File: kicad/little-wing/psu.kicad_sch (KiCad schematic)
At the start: 9 parts, among them J1 ${ALTIUM_VALUE}, U1 ${ALTIUM_VALUE}

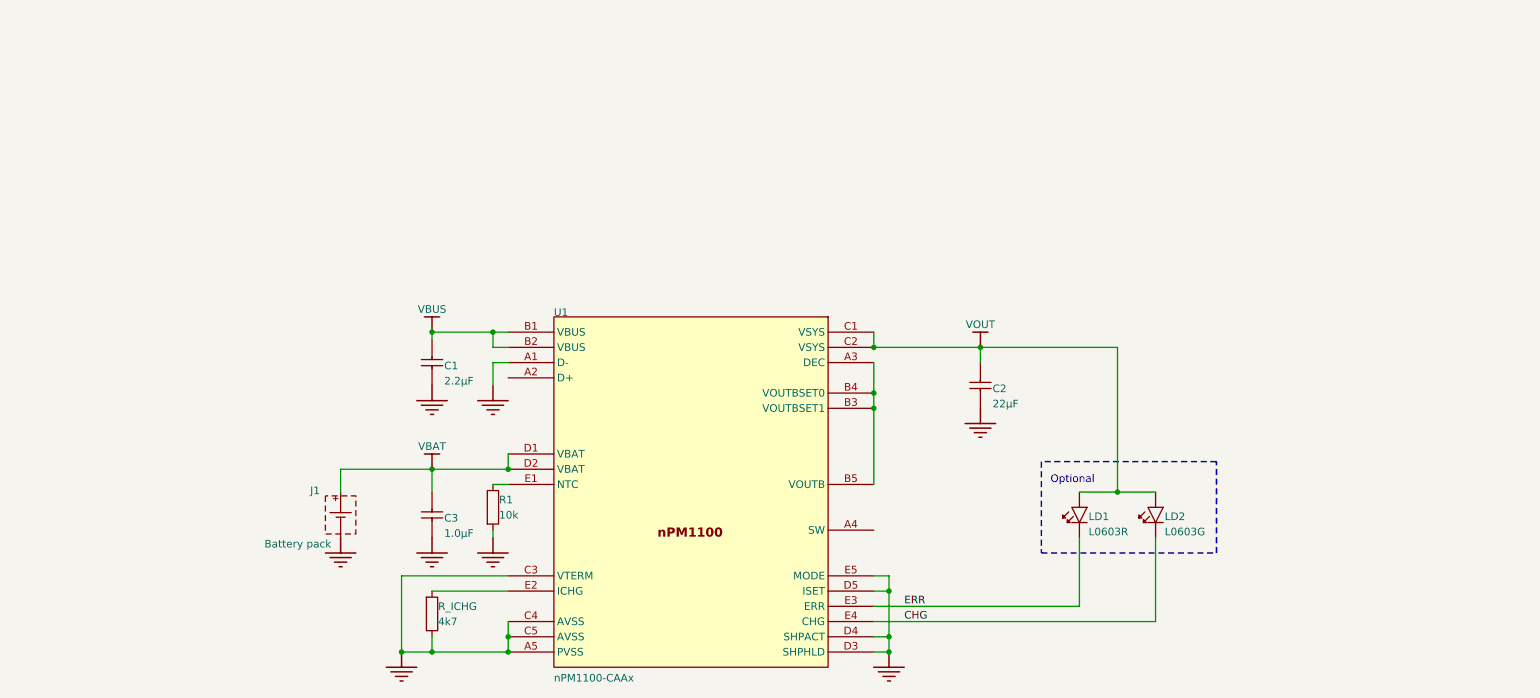
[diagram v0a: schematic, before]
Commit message: Re-shuffling the schematics across sub-sheets
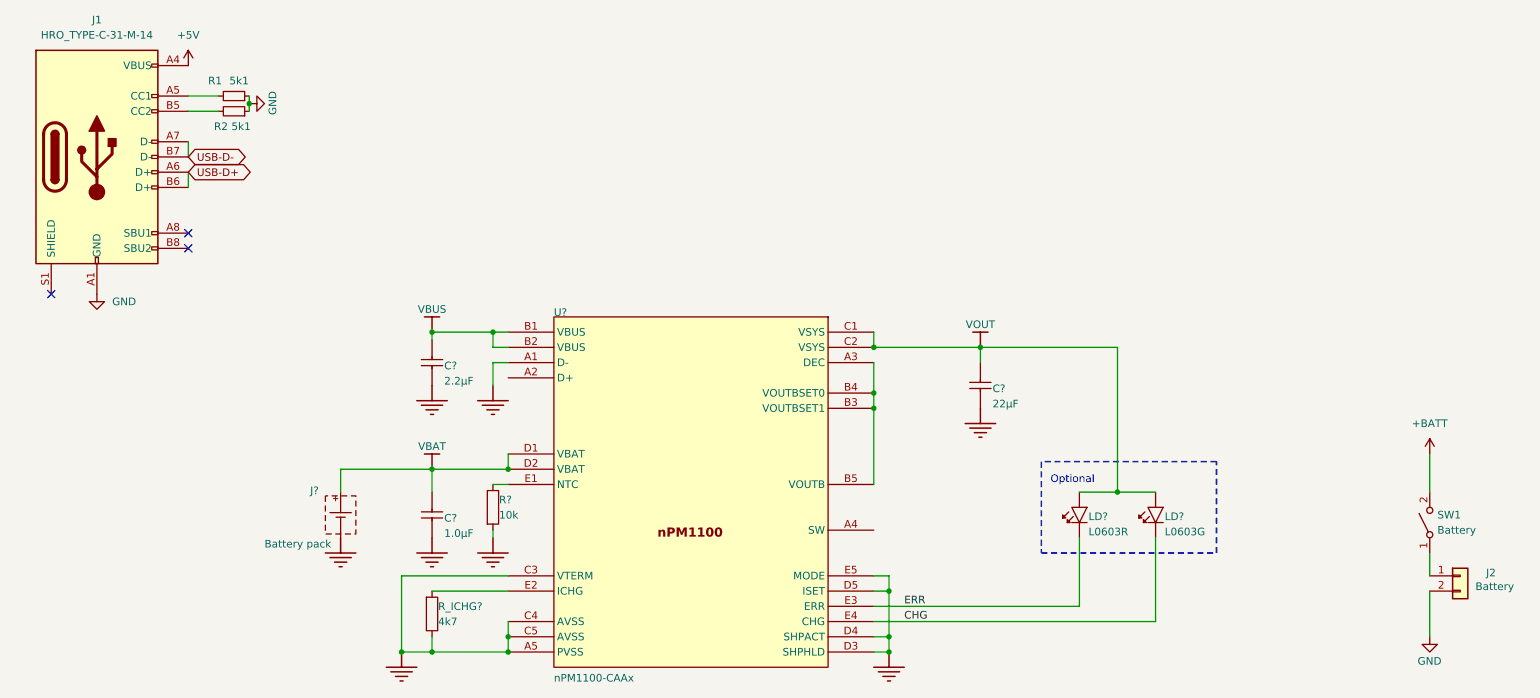
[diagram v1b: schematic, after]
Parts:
- added J1: HRO_TYPE-C-31-M-14, Connector_USB:USB_C_Receptacle_HRO_TYPE-C-31-M-12, symbol Connector:USB_C_Receptacle_USB2.0
- added J2: Battery, Connector_JST:JST_SH_SM02B-SRSS-TB_1x02-1MP_P1.00mm_Horizontal, symbol Connector_Generic:Conn_01x02
- added R1, R2: 5k1, Resistor_SMD:R_0402_1005Metric, symbol Device:R_Small
- added SW1: Battery, symbol Switch:SW_SPST
- renumbered C1 to C?, C2 to C?, C3 to C?, J1 to J?, LD1 to LD?, LD2 to LD?, R1 to R?, R_ICHG to R_ICHG?, U1 to U?
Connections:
- net GND: now also J1.A1 (GND), J1.A12 (GND), J1.B1 (GND), J1.B12 (GND), J2.2 (Pin_2), R1.1, R2.1
- new net: J2.1 (Pin_1), SW1.1 (A)
- new net: J1.A5 (CC1), R1.2
- new net: J1.B5 (CC2), R2.2
- new net +5V: J1.A4 (VBUS), J1.A9 (VBUS), J1.B4 (VBUS), J1.B9 (VBUS)
- new net +BATT: SW1.2 (B)
- new net USB-D+: J1.A6 (D+), J1.B6 (D+)
- new net USB-D-: J1.A7 (D-), J1.B7 (D-)
- no-connect marks 0 -> 3

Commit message: Tidying up the mess a little bit
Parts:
- removed J?: ${ALTIUM_VALUE}, TP_2x1mm_TH, symbol AltiumLib:root_0_Battery_pack_AltiumLib.DbLib
- gave numbers to parts that had none: 8
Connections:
- net +BATT is gone; now on net VBAT: SW1.2 (B)

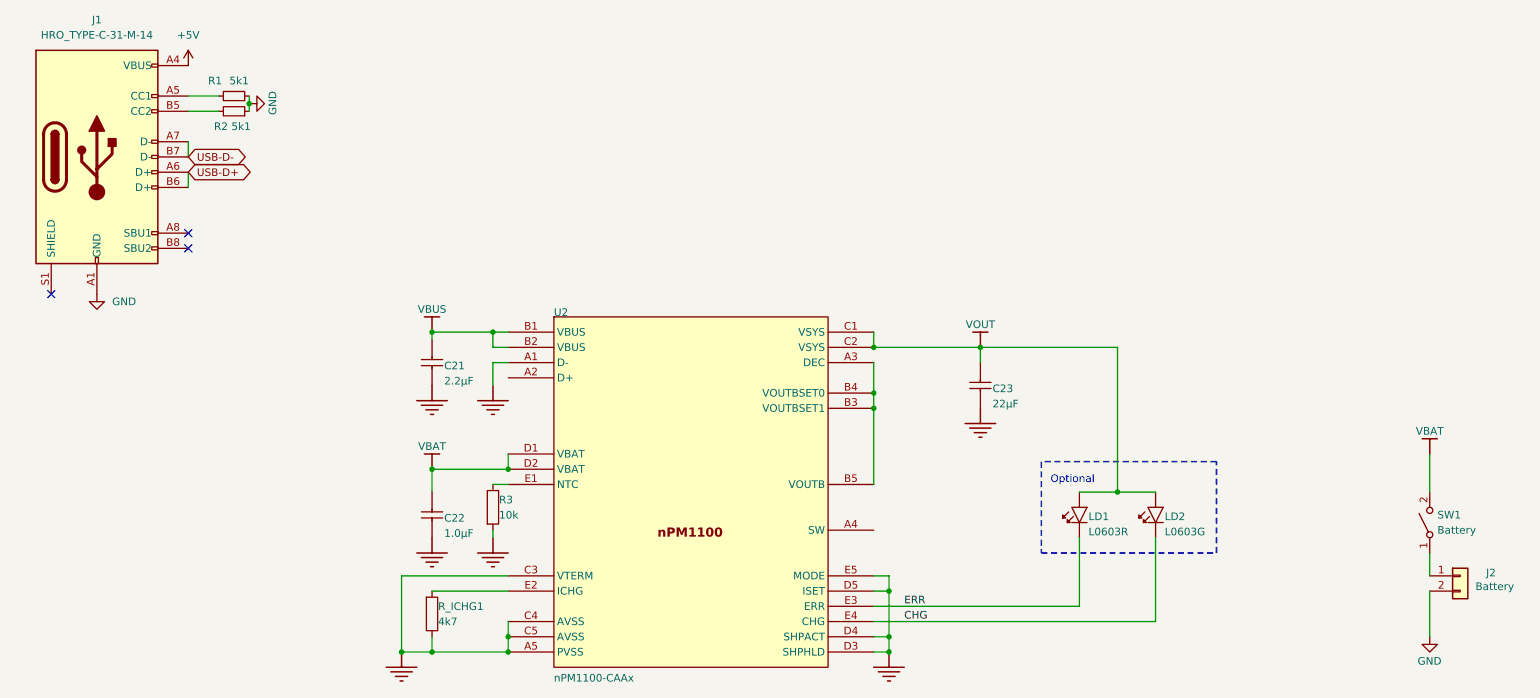
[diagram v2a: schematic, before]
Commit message: Cleaning up the PSU schematics
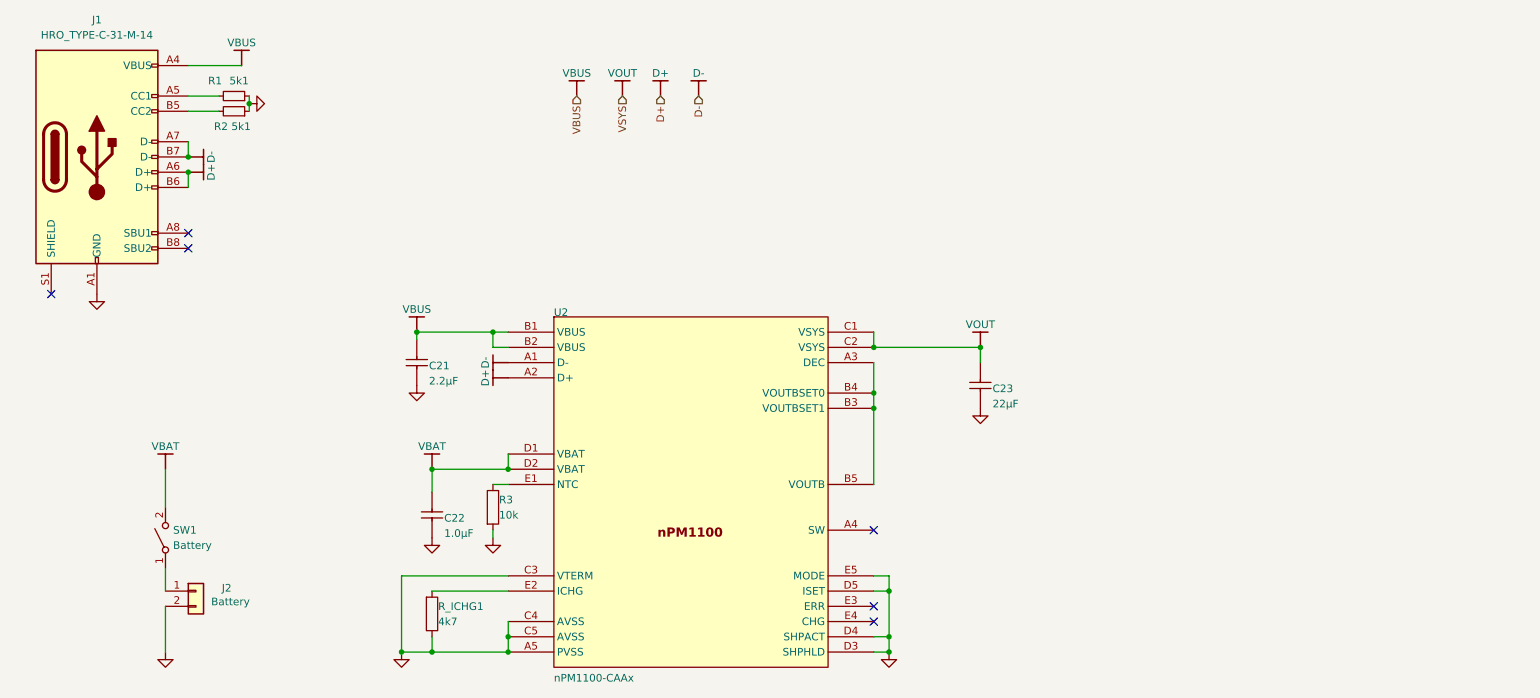
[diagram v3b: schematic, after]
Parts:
- removed LD1: ${ALTIUM_VALUE}, LED_0603_R, symbol AltiumLib:root_3_mirrored_D{colon}LED_AltiumLib.DbLib
- removed LD2: ${ALTIUM_VALUE}, LED_0603_G, symbol AltiumLib:root_3_mirrored_D{colon}LED_AltiumLib.DbLib
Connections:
- net +5V is gone; now on net VBUS: J1.A4 (VBUS), J1.A9 (VBUS), J1.B4 (VBUS), J1.B9 (VBUS)
- net USB-D+ is gone; now on net D+: J1.A6 (D+), J1.B6 (D+)
- net GND: no longer U2.A1 (D-)
- net D+: now reaches U2.A2 (D+)
- net CHG: no longer names the net of U2.E4 (CHG)
- net ERR: no longer names the net of U2.E3 (ERR)
- net USB-D- renamed D-
- net D-: now also U2.A1 (D-)
- no-connect marks 3 -> 6
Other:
- note removed: "Optional"
- moved on the sheet: C21, J2, SW1

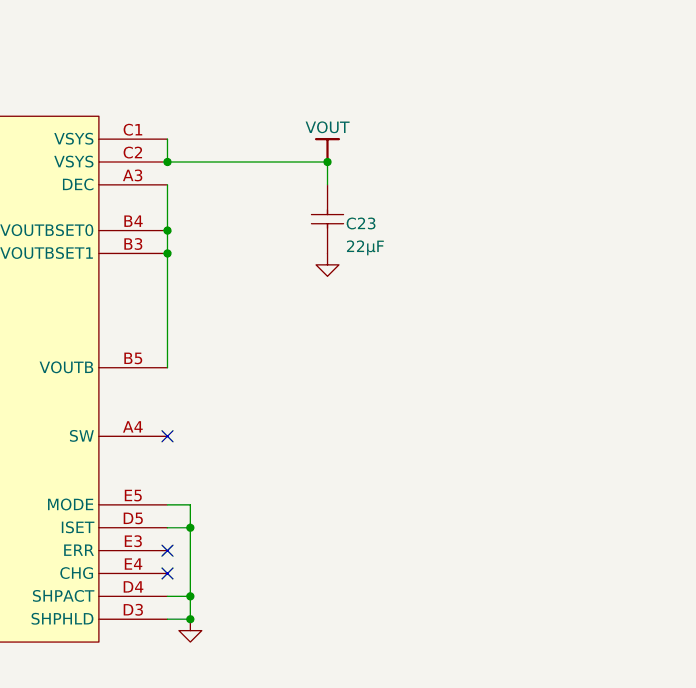
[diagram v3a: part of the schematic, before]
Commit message: Cleaning up the schematics a bit more
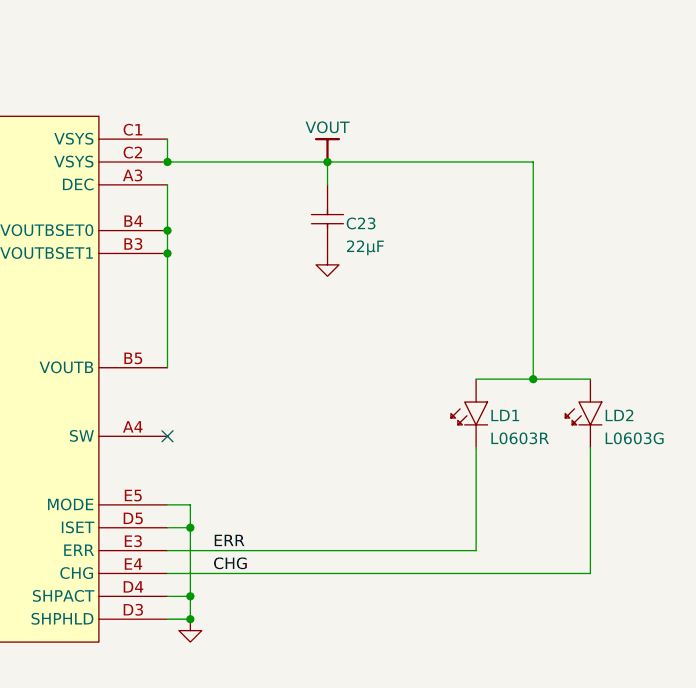
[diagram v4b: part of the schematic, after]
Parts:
- added LD1: ${ALTIUM_VALUE}, LED_0603_R, symbol AltiumLib:root_3_mirrored_D{colon}LED_AltiumLib.DbLib
- added LD2: ${ALTIUM_VALUE}, LED_0603_G, symbol AltiumLib:root_3_mirrored_D{colon}LED_AltiumLib.DbLib
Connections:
- net VOUT: now also LD1.2 (A), LD2.2 (A)
- net ERR: now reaches U2.E3 (ERR)
- net ERR: now also LD1.1 (C)
- net CHG: now reaches U2.E4 (CHG)
- net CHG: now also LD2.1 (C)
- no-connect marks 6 -> 4

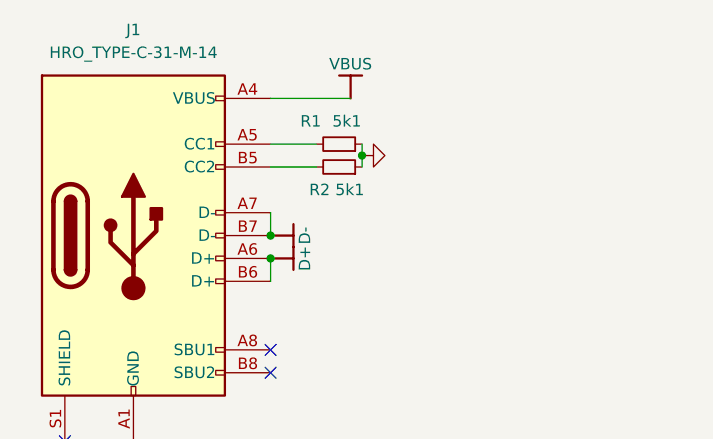
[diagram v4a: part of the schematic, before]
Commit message: Updating schematics/pcb to match the labels
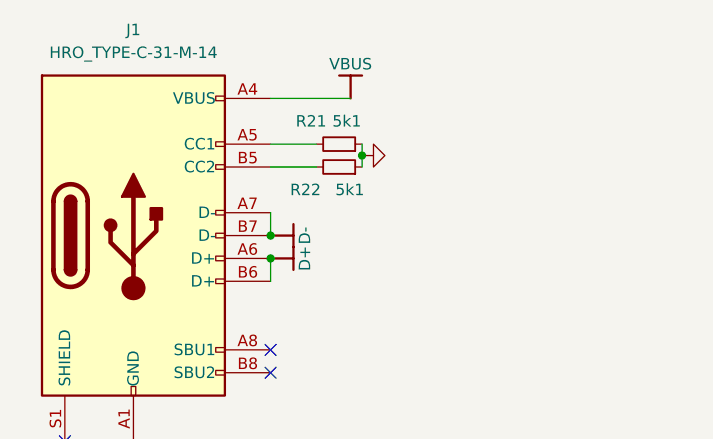
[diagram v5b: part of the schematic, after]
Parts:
- renumbered R1 to R21, R2 to R22
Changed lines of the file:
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@@
 		(on_board yes)
 		(dnp no)
-		(property "Reference" "R1"
-			(at 54.102 30.48 90)
+		(property "Reference" "R21"
+			(at 53.594 30.48 90)
 			(effects
 				(font
@@
 			(project "little-wing"
 				(path "/3a835e6f-a660-4b38-a102-87841cdd95ed/eaaf4618-ba3d-41b4-8a99-4f719e243661/4bfeadaf-0d2e-45fd-a340-a53ab79162c6"
-					(reference "R1")
+					(reference "R21")
 					(unit 1)
 				)
@@
 		(on_board yes)
 		(dnp no)
-		(property "Reference" "R2"
-			(at 57.404 38.1 90)
+		(property "Reference" "R22"
+			(at 56.388 38.1 90)
 			(effects
 				(font
@@
 			(project "little-wing"
 				(path "/3a835e6f-a660-4b38-a102-87841cdd95ed/eaaf4618-ba3d-41b4-8a99-4f719e243661/4bfeadaf-0d2e-45fd-a340-a53ab79162c6"
-					(reference "R2")
-					(unit 1)
-				)
+					(reference "R22")
+					(unit 1)
+				)

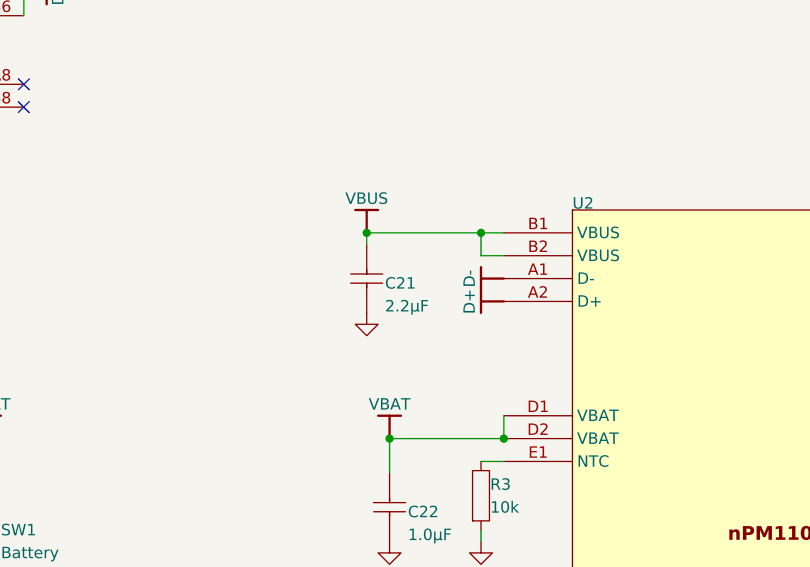
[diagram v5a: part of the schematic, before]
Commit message: Cleaning up some space on the PCB
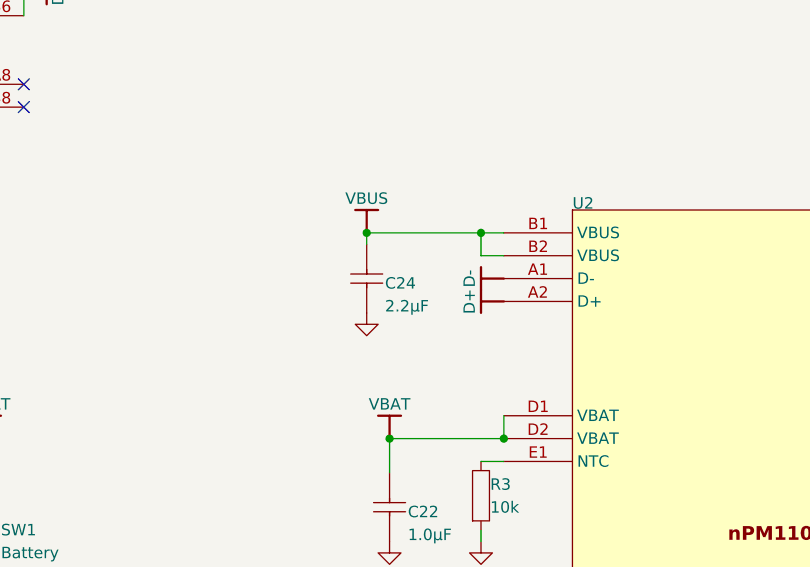
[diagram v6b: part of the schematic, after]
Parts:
- renumbered C21 to C24
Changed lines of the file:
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@@
 		(on_board yes)
 		(dnp no)
-		(property "Reference" "C21"
+		(property "Reference" "C24"
 			(at 90.932 78.74 0)
 			(effects
@@
 			(project "little-wing"
 				(path "/3a835e6f-a660-4b38-a102-87841cdd95ed/eaaf4618-ba3d-41b4-8a99-4f719e243661/4bfeadaf-0d2e-45fd-a340-a53ab79162c6"
-					(reference "C21")
+					(reference "C24")
 					(unit 1)
 				)

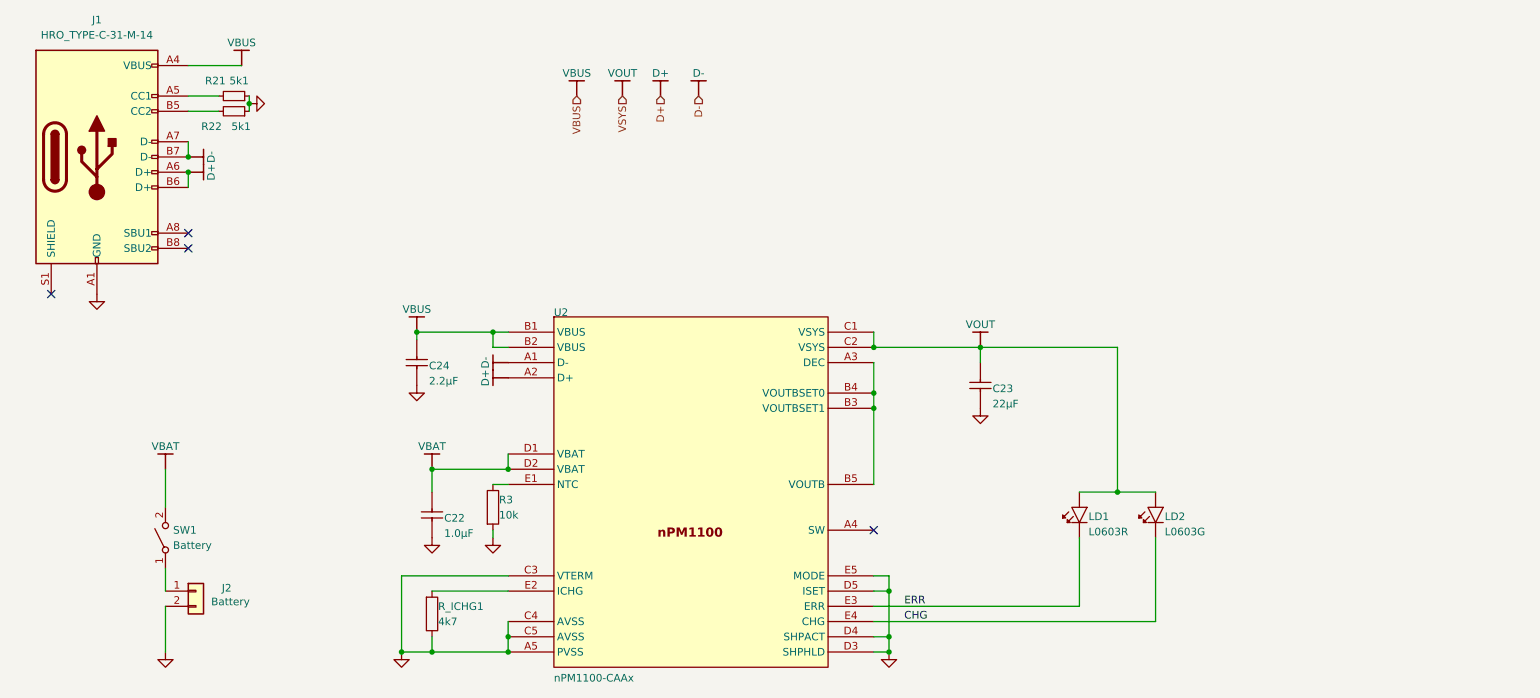
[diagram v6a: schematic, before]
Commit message: Reseting all the extra components sizes
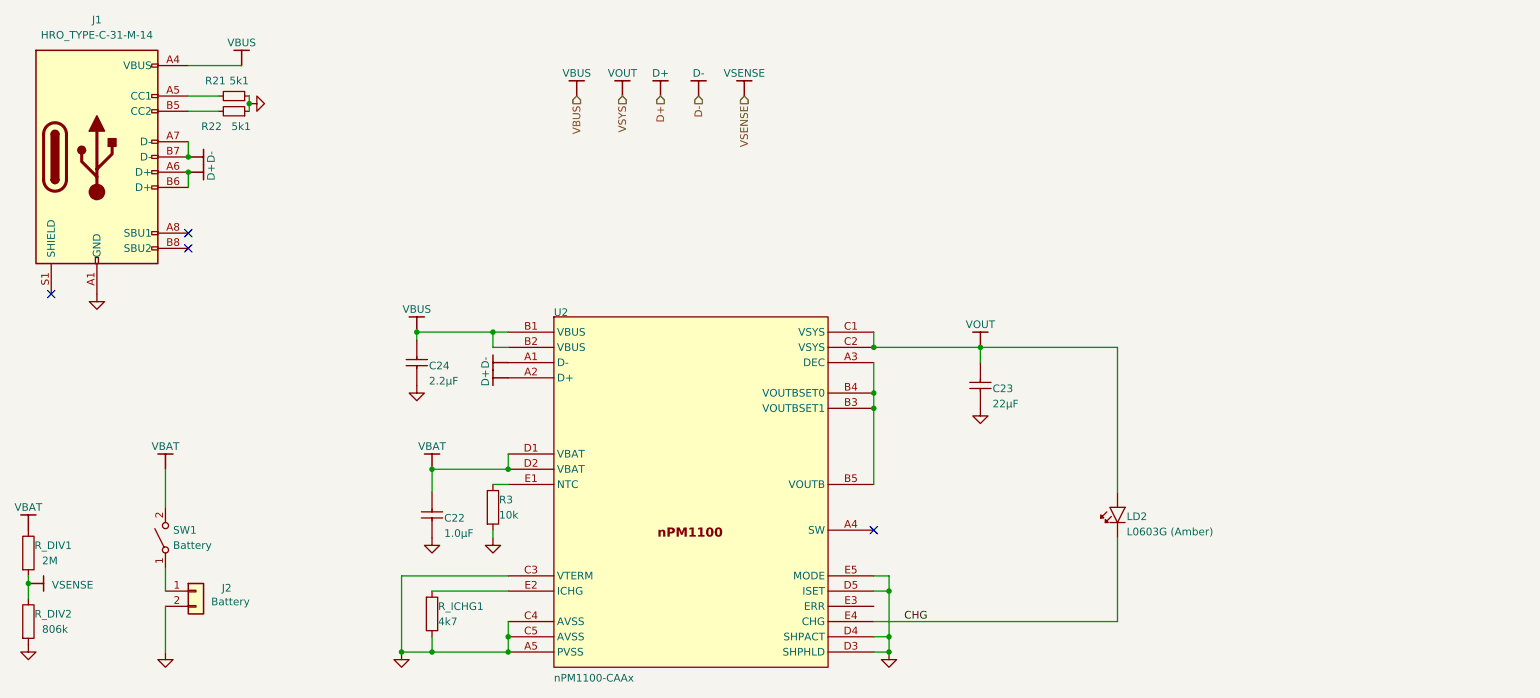
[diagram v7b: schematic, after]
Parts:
- removed LD1: ${ALTIUM_VALUE}, LED_0603_R, symbol AltiumLib:root_3_mirrored_D{colon}LED_AltiumLib.DbLib
- added R_DIV1: 2M, Resistor_SMD:R_0201_0603Metric, symbol AltiumLib:root_3_mirrored_RES_AltiumLib.DbLib
- added R_DIV2: 806k, Resistor_SMD:R_0201_0603Metric, symbol AltiumLib:root_3_mirrored_RES_AltiumLib.DbLib
- LD2: value ${ALTIUM_VALUE} -> L0603G (Amber); footprint LED_0603_G -> LED_SMD:LED_0201_0603Metric
- R21, R22: footprint Resistor_SMD:R_0402_1005Metric -> Resistor_SMD:R_0201_0603Metric
- R3, R_ICHG1: footprint RESC0603X03L_C -> Resistor_SMD:R_0201_0603Metric
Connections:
- net GND: now also R_DIV2.2
- net VBAT: now also R_DIV1.1
- net ERR: no longer names the net of U2.E3 (ERR)
- new net VSENSE: R_DIV1.2, R_DIV2.1
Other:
- moved on the sheet: LD2
